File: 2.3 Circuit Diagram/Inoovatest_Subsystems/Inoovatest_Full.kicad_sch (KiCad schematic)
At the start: 111 parts, among them IC1 MCP73223, IC2 MAX6126, J1 M12 5-pin, J2 USB_A, J3 USB_C Charging port, Q1 AO3401A, Q2 AO3401A, Q3 AO3400A, Q4 AO3400A, Q5 AO3401A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

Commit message: Schematic Export to the Document
- Wassim's annotations and some extra exported and added to the word document
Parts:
- R4: value 100kΩ -> 24.2kΩ
- U5: value MOC 8102 Optocoupler -> MOC8102
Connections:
- net at IC1.6 (STATS1): now also D2.3 (K2)
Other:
- note added: "10V Boost Converter"
- note added: "3.3V Buck Converter"
- note added: "5.5V Boost Converter"
- note added: "5V Boost Converter"
- note added: "LCD Controller"
- note added: "Li-Ion Battery"
- note added: "Linear Charging Controller"
- note added: "MCU"
- note added: "Optocoupler"
- note added: "Power MOSFET"
- note added: "Selectable Excitation Rails"
- note added: "USB-C Port"
- note added: "Voltage Reference"
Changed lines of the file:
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@@
 		)
 	)
-	(text "Li-Po Battery\n"
+	(text "Li-Ion Battery\n"
 		(exclude_from_sim no)
-		(at 73.406 171.704 0)
+		(at 71.882 187.706 0)
+		(effects
+			(font
+				(size 1.27 1.27)
+			)
+		)
+	)
+	(text "5V Boost Converter"
+		(exclude_from_sim no)
+		(at 68.326 268.732 0)
 		(effects
 			(font
@@
 		)
 	)
+	(text "USB-C Port\n"
+		(exclude_from_sim no)
+		(at 26.416 153.67 0)
+		(effects
+			(font
+				(size 1.27 1.27)
+			)
+		)
+	)
 	(text "Analog\nSupply\n"
 		(exclude_from_sim no)
@@
 		)
 	)
+	(text "Power MOSFET"
+		(exclude_from_sim no)
+		(at 115.57 204.724 0)
+		(effects
+			(font
+				(size 1.27 1.27)
+			)
+		)
+	)
+	(text "Selectable Excitation Rails"
+		(exclude_from_sim no)
+		(at 53.848 18.796 0)
+		(effects
+			(font
+				(size 1.27 1.27)
+			)
+		)
+	)
 	(text "Battery Management System"
 		(exclude_from_sim no)
@@
 		)
 	)
+	(text "3.3V Buck Converter"
+		(exclude_from_sim no)
+		(at 173.482 234.188 0)
+		(effects
+			(font
+				(size 1.27 1.27)
+			)
+		)
+	)
+	(text "Voltage Reference"
+		(exclude_from_sim no)
+		(at 105.41 38.354 0)
+		(effects
+			(font
+				(size 1.27 1.27)
+			)
+		)
+	)
+	(text "Optocoupler\n"
+		(exclude_from_sim no)
+		(at 170.18 197.104 0)
+		(effects
+			(font
+				(size 1.27 1.27)
+			)
+		)
+	)
 	(text "Delta-Sigma ADC"
 		(exclude_from_sim no)
@@
 		)
 	)
+	(text "5.5V Boost Converter"
+		(exclude_from_sim no)
+		(at 162.306 277.876 0)
+		(effects
+			(font
+				(size 1.27 1.27)
+			)
+		)
+	)
+	(text "10V Boost Converter"
+		(exclude_from_sim no)
+		(at 65.786 224.028 0)
+		(effects
+			(font
+				(size 1.27 1.27)
+			)
+		)
+	)
 	(text "+"
 		(exclude_from_sim no)
@@
 		)
 	)
+	(text "LCD Controller"
+		(exclude_from_sim no)
+		(at 271.272 187.706 0)
+		(effects
+			(font
+				(size 1.27 1.27)
+			)
+		)
+	)
 	(text "USB-A MODULE\n"
 		(exclude_from_sim no)
@@
 		)
 	)
+	(text "MCU"
+		(exclude_from_sim no)
+		(at 321.564 117.856 0)
+		(effects
+			(font
+				(size 1.27 1.27)
+			)
+		)
+	)
 	(text "unidirectional tvs diode"
 		(exclude_from_sim no)
@@
 		)
 	)
+	(text "Linear Charging Controller"
+		(exclude_from_sim no)
+		(at 93.98 139.954 0)
+		(effects
+			(font
+				(size 1.27 1.27)
+			)
+		)
+	)
 	(text "From \nCharging Circuit\n"
 		(exclude_from_sim no)
@@
 		)
 		(property "Value" "Battery Terminal"
-			(at 73.152 187.706 0)
+			(at 79.502 170.434 0)
 			(effects
 				(font
@@
 		(dnp no)
 		(property "Reference" "U5"
-			(at 158.75 182.626 0)
+			(at 168.656 179.832 0)
 			(effects
 				(font
@@
 			)
 		)
-		(property "Value" "MOC 8102 Optocoupler"
-			(at 173.99 181.356 0)
+		(property "Value" "MOC8102"
+			(at 168.91 181.864 0)
 			(effects
 				(font
@@
 		(dnp no)
 		(property "Reference" "R19"
-			(at 37.338 207.518 0)
+			(at 35.814 207.518 0)
 			(effects
 				(font
@@
 			)
 		)
-		(property "Value" "100kΩ"
-			(at 145.288 145.288 0)
+		(property "Value" "24.2kΩ"
+			(at 146.304 145.542 0)
 			(effects
 				(font
@@
 		(dnp no)
 		(property "Reference" "R21"
-			(at 39.37 217.932 0)
+			(at 39.878 217.932 0)
 			(effects
 				(font

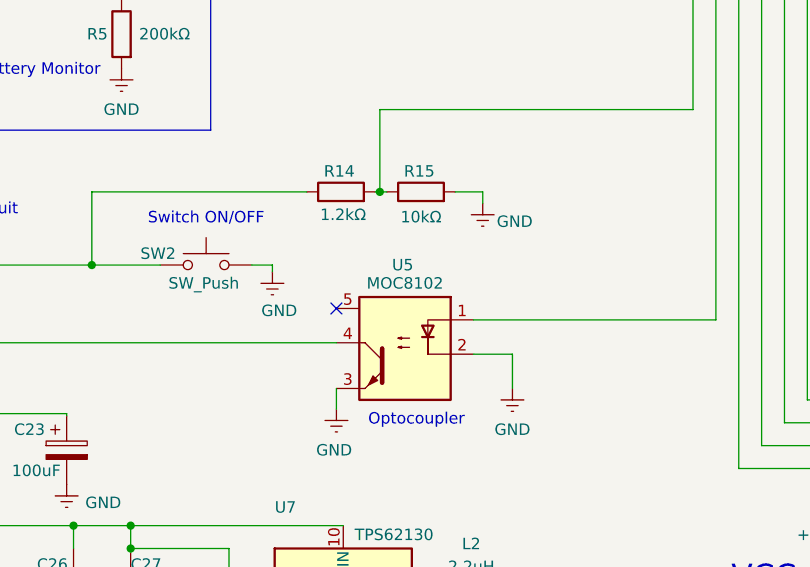
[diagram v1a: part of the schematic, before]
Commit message: Minor Updates
- changed the optocoupler since it was a bit outdated
- reworked battery estimate and it's still only 7 hours
- from Okan: 2nd draft of User Manual
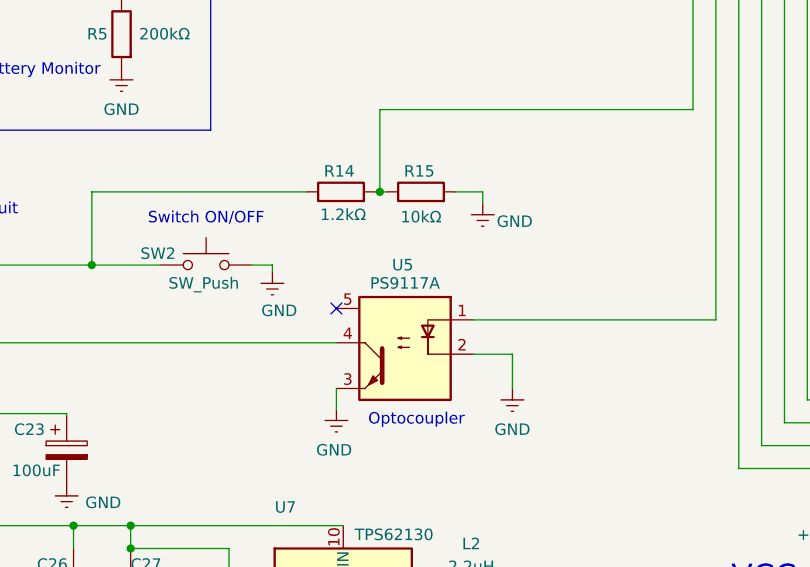
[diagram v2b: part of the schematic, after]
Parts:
- U5: value MOC8102 -> PS9117A
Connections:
- net at IC1.6 (STATS1): now also D2.3 (K2)
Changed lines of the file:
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@@
 			)
 		)
-		(property "Value" "MOC8102"
+		(property "Value" "PS9117A"
 			(at 168.91 181.864 0)
 			(effects
